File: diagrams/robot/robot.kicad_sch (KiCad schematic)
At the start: 1 part, among them U1 ESP32-WROOM-32

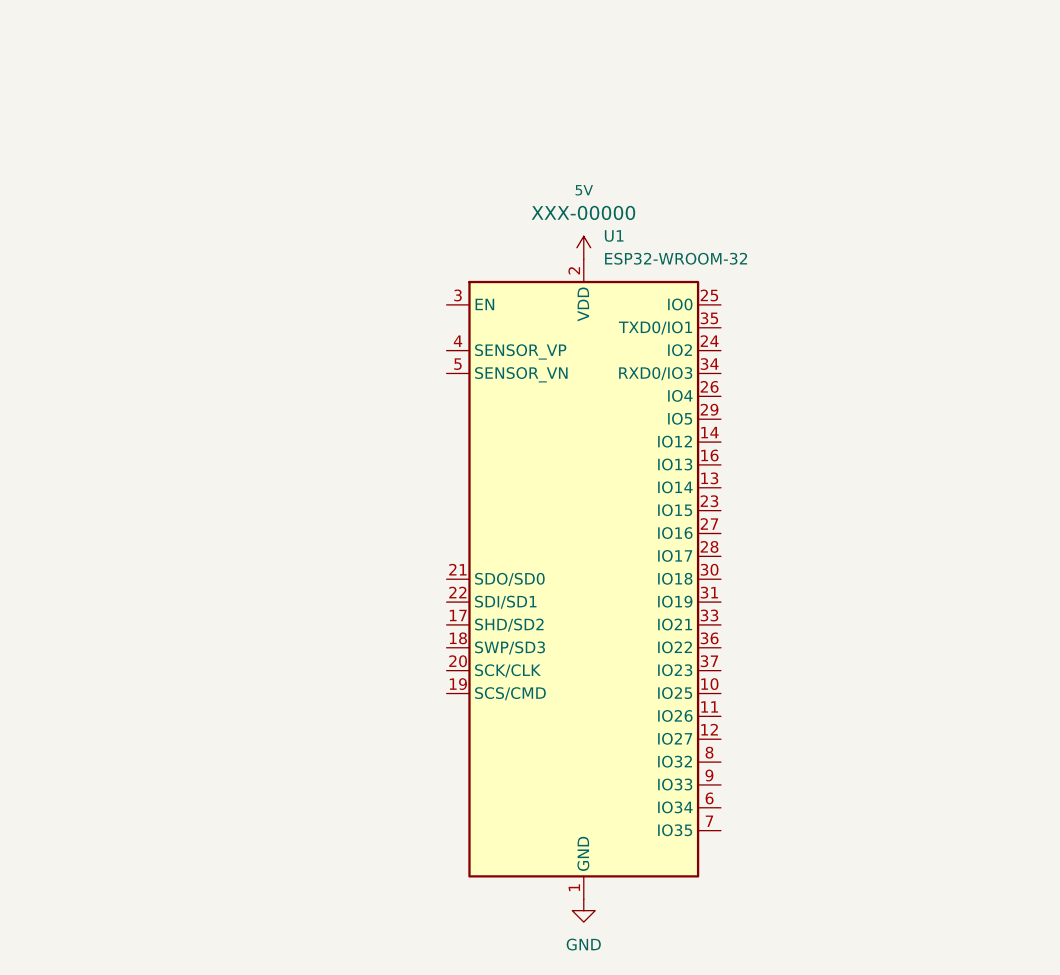
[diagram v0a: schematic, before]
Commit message: "Added sleep and battery management functionality"
Updated several files to include power management functionalities as well as adjustments necessary for proper communication between the controller and car modules.

In "config.h" file, introduced new variables for battery pin, and changed the broadcast address for communication. Adjusted timer configurations for proper sleep intervals.

In "State.h" and "State.cpp" files, introduced validity checks and sleep flags to manage controller behavior. Replaced the Timer0_ISR method to handle a goToSleep flag which can be used to place the device into deep sleep mode.

In the "main.cpp" files in both car and controller module, incorporated new logic for initializing and adjusting for battery reading, while also including clean up and sleeping when needed.

Also updated robot diagrams to reflect changes in circuitry and information transmission.

These changes are crucial for correct controller behavior and power conservation. Also optimized movement commands for smoother vehicle operation.
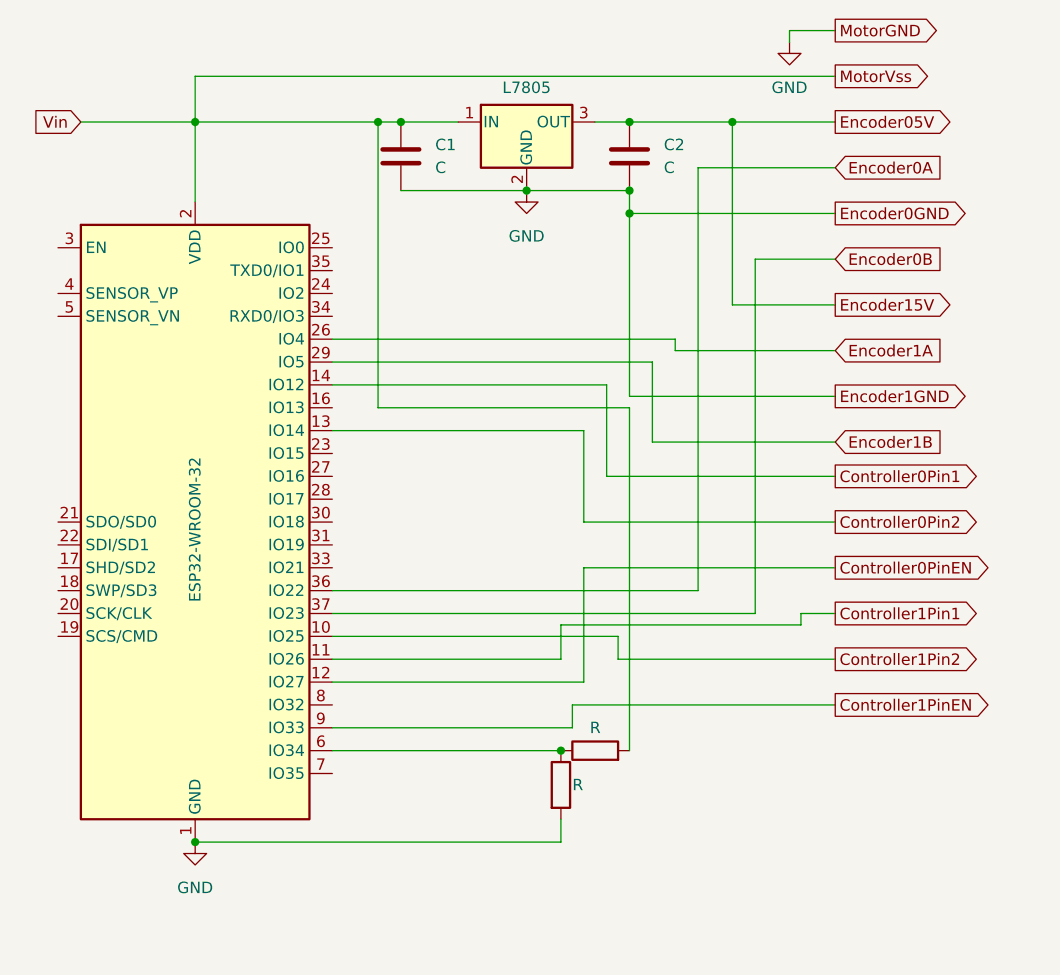
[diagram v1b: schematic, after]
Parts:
- added C1, C2: C, symbol Device:C
- added R1, R2: R, symbol Device:R
- added U2: L7805, symbol Regulator_Linear:L7805
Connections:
- net GND: now also C1.2, C2.2, R1.2, U2.2 (GND)
- net Controller1Pin2: now reaches U1.10 (IO25)
- net Controller1Pin1: now reaches U1.11 (IO26)
- net Controller0PinEN: now reaches U1.12 (IO27)
- net Controller0Pin2: now reaches U1.13 (IO14)
- net Controller0Pin1: now reaches U1.14 (IO12)
- net Encoder1A: now reaches U1.26 (IO4)
- net Encoder1B: now reaches U1.29 (IO5)
- net Encoder0A: now reaches U1.36 (IO22)
- net Encoder0B: now reaches U1.37 (IO23)
- net at U1.6 (IO34): now also R1.1, R2.1
- net Controller1PinEN: now reaches U1.9 (IO33)
- net 5V renamed MotorVss
- net MotorVss: now also C1.1, R2.2, U2.1 (IN)
- new net Encoder05V: C2.1, U2.3 (OUT)
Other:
- title: (none) -> Robot
